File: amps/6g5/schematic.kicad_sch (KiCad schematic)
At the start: 98 parts, among them SW1 AC

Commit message: Fix: 6G5 tone network redrawn from the A-FJ sheet — it is the 6G4's, part for part; taper letters corrected
- The sheet draws the 6G4 network exactly: .05 coupler, 100K slope, 250MM
  treble capacitor, a Bass DIVIDER with .01 across its upper section and 10K
  across its lower, the Treble wiper into the Volume pot, 47MM across it.
- The drawing had no slope resistor and no coupler, and put the 10K in series
  with the .01 between the plate and the stack — while bom.yaml's own role for
  that 10K read "tone network foot". Parts list and drawing contradicted each
  other about the same part.
- Parts list: CC1T/CC2T .05, RS1T/RS2T 100K, CBR1/CBR2 47 pF added; CF/RF roles
  rewritten. And two taper letters corrected to what BOTH pages of the drawing
  print: Treble 250K-L (was 250 kΩ-A) and Volume 500K-L (was 250 kΩ-A, with a
  note about "two candidate tapers" that the sheet does not carry). Every
  surface agrees (check_value_consistency --strict clean).
- Board: this layout placed no tone parts at all ("schematic-only"). Now the
  couplers stand at the plate eyelets and the Treble and Bass pots and the
  parts the layout page hangs at each pot are drawn on the panel row and wired
  lug to lug; the board is widened to 51 columns so the two control groups fit
  without moving any existing board part. Hand-routed to zero findings, then
  tidied by the route helper (which also eased seven pre-existing leads in the
  output section by a fraction of a column). verify_layout_nets PASS (claimed).
- Circuit story: the network as the sheet draws it, the taper correction
  recorded, and the three repo-path leaks (voltages.yaml ×2, netlist.cir)
  rewritten in visitor voice; the sheet notes likewise.
- Social cards and their manifest regenerated for all three repaired boards.

Co-Authored-By: Claude Fable 5.1 <noreply@anthropic.com>
Claude-Session: https://claude.ai/code/session_01KBMfdh37HmCL2iWcBiL5J1
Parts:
- removed CF4: 20u 600V, symbol cx:C
- removed CFB1: .0025u, symbol cx:C
- removed CT2: 250p, symbol cx:C
- removed R2N: 68k, symbol cx:R
- removed RD1: 56k 1W, symbol cx:R
- removed RF2: 10k, symbol cx:R
- removed RG2A, RG5: 1M, symbol cx:R
- removed RPRES: 1.5k, symbol cx:R
- removed V1B, V3, V5, V6A: 7025, symbol cx:TRIODE
- removed V7: 6L6GC, symbol cx:PENTODE
- added CBR1, CBR2: 47p, symbol cx:C
- added CC2T: .05u, symbol cx:C
- added CF2, CTO1: .01u, symbol cx:C
- added CF6: 20u 600V, symbol cx:C
- added CK1B: 25u (info.), symbol cx:C
- added CPRES: .1u 200V, symbol cx:C
- added CT1: 250p, symbol cx:C
- added JSPK: spkr, symbol cx:JACK
- added RFB1: 470k, symbol cx:R
- added RGA: 1M, symbol cx:R
- added RK2A, RK5: 820, symbol cx:R
- added RS1T, RTOP: 100k, symbol cx:R
- added SW1: AC, symbol cx:SWITCH
- added V2A: 7025, symbol cx:TRIODE
- added VRB2: 250k-A, symbol cx:POT
- added VRSPD: 4M-RA speed, symbol cx:POT
- CC1T: renamed from CT1; value 250p -> .05u
- CFB1: renamed from CTO1; value .01u -> .0025u
- CMIX2: renamed from RK5; value 820 -> .05u; symbol cx:R -> cx:C
- CT2: renamed from CF2; value .01u -> 250p
- R2N: renamed from V2A; value 7025 -> 68k; symbol cx:TRIODE -> cx:R
- RD1: renamed from SW1; value AC -> 56k 1W; symbol cx:SWITCH -> cx:R
- RF2: renamed from RL2B; value 100k -> 10k
- RFB2: renamed from RTOP; value 100k -> 220k
- RG2A: renamed from RK2A; value 820 -> 1M
- RG5: renamed from RFB1; value 470k -> 1M
- RL2B: renamed from CMIX2; value .05u -> 100k; symbol cx:C -> cx:R
- RPRES: renamed from RGA; value 1M -> 1.5k
- RS2T: renamed from VRB2; value 250k-A -> 100k; symbol cx:POT -> cx:R
- RSC2: renamed from JSPK; value spkr -> 470 1W; symbol cx:JACK -> cx:R
- RTAIL: renamed from CPRES; value .1u 200V -> 820; symbol cx:C -> cx:R
- V1B: renamed from CK1B; value 25u (info.) -> 7025; symbol cx:C -> cx:TRIODE
- V3: renamed from VRSPD; value 4M-RA speed -> 7025; symbol cx:POT -> cx:TRIODE
- V5: renamed from RFB2; value 220k -> 7025; symbol cx:R -> cx:TRIODE
- V6A: renamed from RTAIL; value 820 -> 7025; symbol cx:R -> cx:TRIODE
- V7: renamed from RSC2; value 470 1W -> 6L6GC; symbol cx:R -> cx:PENTODE
- VRT1, VRT2: value 250k-A -> 250k-L
- VRV1, VRV2: value 250k-A -> 500k-L
- renumbered CF6 to CF4
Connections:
- net BD: now also RL2B.1; no longer RF2.1
- net BP1: now also CF4.1, RTOP.1; no longer RFB2.1
- net BP2: now also RD1.1, RSC2.2; no longer V7.2
- net BP3: now also RD1.2, CF6.1; no longer CF4.1
- net BRT 1: now also RG2A.1, V2A.2 (G)
- net BRT 2: now also R2N.1
- net GND: now also CFB1.1, RF1.2, RF2.2, RFB2.2, RG5.2, RPRES.2, V7.4 (K), CF6.2, CK1B.2, CPRES.2, RK2A.2, RK5.2, VRB2.3, VRSPD.1, VRSPD.2 (W); no longer CMIX2.2, RS2T.3, RTAIL.2, V1B.2, V3.1, V3.2 (W), V5.2
- net MAINS: now also SW1.1; no longer RD1.1
- net MIXG2: now also CMIX2.2, RG5.1, V5.2 (G); no longer RL2B.2
- net SPKR: now also JSPK.1 (T); no longer RSC2.1 (T)
- net at TR2.5 (SEC_C): now also JSPK.2 (S); no longer RSC2.2 (S)
- net at CTOK.1, D1.1 (A), D2.1 (A)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: now also V3.3 (K)
- net at V2B.2 (G), VRV2.2 (W): now also CBR2.2
- net at F1.1: now also SW1.2; no longer RD1.2
- net at CC1T.1, RL1A.2, V1A.1 (P): no longer RF1.1
- net at RL2A.2: now also CC2T.1, V2A.1 (P); no longer R2N.1 (P)
- net at CMIX2.1: now also RL2B.2, V2B.1 (P); no longer CK5.1
- net at CFB1.2: now also RL5.2, V5.1 (P), RFB1.1; no longer V3.3
- net at CF1.1: now also VRB1.1, VRT1.3, RS1T.2; no longer RF1.2
- net at CTO2.1, RTOG2.2: now also V3.2 (G)
- net at CTO2.2, RTOG1.2: now also CTO1.1; no longer CFB1.1
- net at V8.3 (G2): now also RSC2.1; no longer V7.1
- net at CTO3.2, VRINT.1: now also V3.1 (P), RTOP.2; no longer RFB2.2
- net at CMIX1.1, RL1B.2: now also V1B.1 (P)
- net at RPRES.1: now also RNFB.2, RT2.1, VRPRES.1, VRPRES.2 (W)
- net at RGB.1, RT2.2: now also RTAIL.1, RGA.2; no longer RPRES.2, V6A.1
- net at RK1B.1: now also V1B.3 (K), CK1B.1; no longer V1B.1
- net at VRV1.1: now also CBR1.1; no longer VRT1.2 (W)
- net at VRV1.2 (W): now also V1B.2 (G), CBR1.2
- net at C1.1, CPID.1, RLA.2: now also V6A.1 (P)
- net at C1.2, RGL1.1: now also V7.2 (G1)
- net at V6B.3 (K): now also RTAIL.2, V6A.3 (K); no longer V6A.2
- net at VRPRES.3: now also CPRES.1; no longer RTAIL.1
- net at VRT2.1: now also CT2.2
- net at CC1T.2: now also CT1.1, RS1T.1; no longer VRT1.1
- net at TR2.1 (PRI_A): now also V7.1 (P)
- net at VRT2.2 (W): no longer VRV2.1
- net at RS2T.2, VRT2.3: now also CF2.1, VRB2.1; no longer RS2T.1
- net at CF1.2: now also RF1.1, VRB1.2 (W)
- net at RSC1.1: now also V7.3 (G2)
- net at CT2.1: now also RS2T.1, CC2T.2
- new net: RFB1.2, RFB2.1, RFB3.2
- new net: CTO1.2, VRSPD.3
- new net: RGA.1, V6A.2 (G)
- new net: CF2.2, RF2.1, VRB2.2 (W)
- new net: CT1.2, VRT1.1
- new net: CBR2.1, VRV2.1
- new net: CK2A.1, RK2A.1, V2A.3 (K)
- new net: CK5.1, RK5.1, V5.3 (K)
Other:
- note added: "Bias supply — a filtered tap this drawing does not fully resolve; the netlist treats -55 V as an ideal source (see the circuit story)"
- note added: "Driver — local feedback network read from the drawing but not confidently resolved (schematic-only; see the circuit story and the parts list)"
- note added: "Heaters, PT primary/mains, pilot lamp and chassis switches are omitted here — see the netlist, the sources list and the board drawing. BP3/BDRV/BD are DRIVEN anchors, not derived through the dropper chain shown (see the circuit story)."
- note added: "Mains cord not drawn — annotation layer (see the board drawing)"
- note added: "Phase-shift ladder values (RTOG1/RTOG2/CTO1-3) are a schematic-only reading, typical of this circuit family — not confidently resolved from the scan (see the parts list)."
- note added: "Pilot lamp — fed from the 6.3 V heater chain (the board drawing's twisted pair)"
- note added: "The tremolo oscillator drives a lamp/photoresistor pair (OPTO) whose photocell shunts the channel-mixing node (see the circuit story)."
- note added: "Tremolo — V3 phase-shift oscillator (DC point excluded from the netlist)"
- note removed: "Bias supply — a filtered tap this drawing does not fully resolve; netlist.cir treats -55 V as an ideal source (notes.md)"
- note removed: "Driver — local feedback network read from the drawing but not confidently resolved (schematic-only; see notes.md, bom.yaml)"
- note removed: "Heaters, PT primary/mains, pilot lamp and chassis switches are omitted here — see netlist.cir, meta.yaml, layout.yaml. BP3/BDRV/BD are DRIVEN anchors, not derived through the dropper chain shown (notes.md)."
- note removed: "Mains cord not drawn — annotation layer (layout.yaml)"
- note removed: "Phase-shift ladder values (RTOG1/RTOG2/CTO1-3) are a schematic-only reading, typical of this circuit family — not confidently resolved from the scan (bom.yaml)."
- note removed: "Pilot lamp — fed from the 6.3 V heater chain (layout.yaml twisted run)"
- note removed: "The tremolo oscillator drives a lamp/photoresistor pair (OPTO) whose photocell shunts the channel-mixing node (notes.md)."
- note removed: "Tremolo — V3 phase-shift oscillator (DC point excluded from netlist.cir)"
- moved on the sheet: CC1T, CF4, CFB1, CK1A, CT2, R1N, RF2, RFB2, RG1A, RG2A, RG5, RK1A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

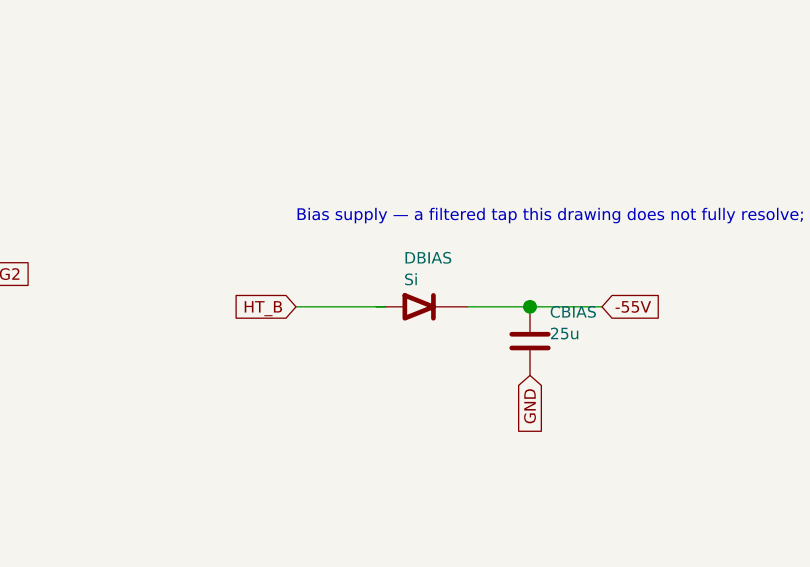
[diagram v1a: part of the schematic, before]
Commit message: Fix: 17 bias rectifiers and six HT diodes drawn backwards; the 6G6-B and 6G4 bias rows as their drawings show; AA1164 V4 units
Rectifier polarity has no gate. The netlists model every supply as an ideal
source, the sheet-vs-board check treats a two-terminal part as unordered, and
the boards' `cathode:` fields were copied from the sheets. Measured over all
68 diodes on 40 sheets: 18 negative-bias rectifiers had the cathode on the
negative node (a diode that way round would charge the node POSITIVE), and all
six 6G6-B HT diodes pointed away from B+. The printed negative bias on each of
those sheets falsifies the drawn orientation; the nine bias rectifiers already
right (AA1164, AA864, AB165, B15N, DR103, JTM100, M1959, M2204, 6G6-B) show
the idiom. Flipped: 5E4-A, 5E5-A, 5E6-A, 5F10, 5F4, 5F6, 5F6-A, 5F8-A, 5G9,
6G2, 6G3, 6G4, 6G5, AA964, AB763, AB763 Super, AB763 Twin, JTM45 (the
M1987's is with the Marshall board repair) and the 6G6-B's DR1-DR6. The
5F8-A board, which had copied its sheet, has the band moved to the tap side;
the other boards' bands are with the board-repair wave. A gate is next.

6G6-B bias. E-FB (6431x3364): the 1K 1W rises from TR1's SECOND secondary
terminal, a bias tap between the upper HT end and the grounded centre tap,
to the diode's + end. The sheet fed the diode from the HT end with the 1K
after it. T1 now carries its tap pin and the row reads tap -> 1K -> diode ->
-54 V. (The triage had read "HT end"; the native crop shows the tap.)

6G4 bias. A-FJ, read natively: tap -> rectifier -> 8 uF -> 10K -> the -55 V
node, which carries a second 8 uF and the 56K to ground as a bleeder. The
sheet fed the rectifier from an HT end, drew the 56K in series and carried
one capacitor. CBIAS2 joins the parts list, and RBIAS1's role now says
bleeder.

AA1164 V4. The K-FD sheet prints the phase inverter 7/6/8 and the tremolo
oscillator 2/1/3 (5554x4346); the sheet had them the other way round.

Gates: check_schematics 40/0 (+selftest), verify_schematic_nets 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
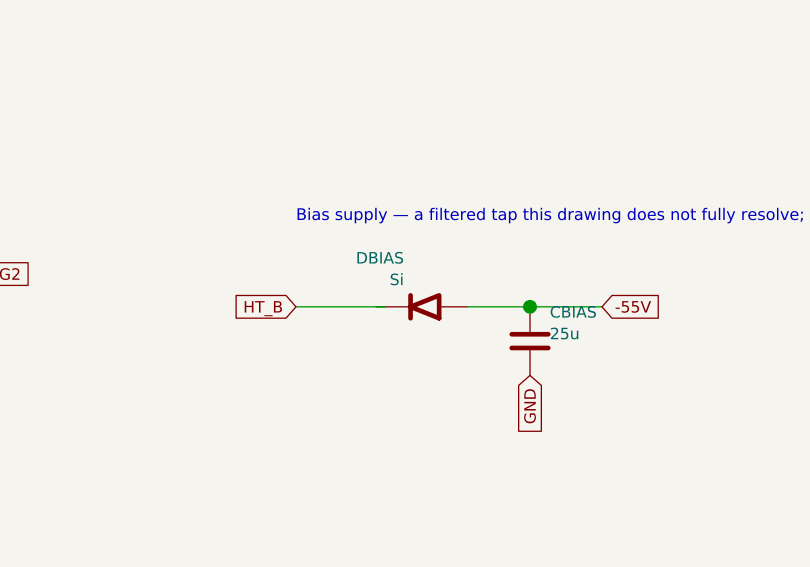
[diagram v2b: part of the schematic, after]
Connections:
- net -55V: now also DBIAS.1 (A); no longer DBIAS.2 (K)
- net HT_B: now also DBIAS.2 (K); no longer DBIAS.1 (A)
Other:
- moved on the sheet: DBIAS
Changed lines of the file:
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@@
   (wire (pts (xy 215.665 206.889) (xy 216.745 206.889))
     (stroke (width 0) (type default)))
-  (symbol (lib_id "cx:DIODE_SS") (at 220.745 206.889 0) (unit 1)
+  (symbol (lib_id "cx:DIODE_SS") (at 220.745 206.889 180) (unit 1)
     (in_bom yes) (on_board yes)
     (property "Reference" "DBIAS" (at 218.745 201.489 0) (effects (font (size 1.27 1.27)) (justify left)))

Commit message: Fix: the 6G5's rectifier was connected to nothing; 17 sheets shorted the mains by naming both leads alike
6G5 power supply. The sheet drew four diodes as a "silicon bridge" whose
HT_A/HT_B labels stopped 6 mm short of their wires. D1/D2's anodes sat on
the tremolo's cathode node (a tremolo wire's end touched the old diode
stub), D3/D4 ran from ground to the reservoir, and TR1's centre tap floated
under an open-pin waiver whose stated reason was the bridge itself.
A-FJ (Schematic Heaven 2153x1437, read enlarged): each HT end of TR1 runs
through a leg of three silicon diodes, every + (cathode) toward the +460 V
reservoir; the centre tap is grounded; TR1's second secondary terminal is a
bias tap feeding the 6G4's network part for part: rectifier, 8-150, 10K,
then 8-150 and a 56K bleeder at the -55 V line. Redrawn as the drawing
shows: D1-D6, TR1 with its tap pin, the centre tap to ground, the bias
network (CBIAS 25 uF -> 8 uF; RBIAS2, CBIAS2, RBIAS1 added), the waiver
deleted, and the notes, meta, netlist header and parts list no longer say
bridge. Not yet carried: the drawing's second 20-600 at the reservoir and
the standby switch (this sheet omits chassis switches by its own note);
and the tremolo ladder still runs through the transformer's corner of the
sheet, a layout clash rather than a connection, queued for its own redraw.

Mains. Two global labels with one name are one net. 16 of 24 power
transformers on the sheets carried a label named MAINS on both primary
leads, so the winding's two pins were one net: 5E4-A, 5E5-A, 5F4, 5G9,
6161, 6G2, 6G3, 6G4, AA1164, AA764, AA764-Vibro, AA964, AB763, AB763
Super, AB763 Twin, GA-40. The 6G5's loop ran from one MAINS label through
switch, fuse and winding back to the same name. No gate models the primary,
so a copy-pasted idiom did this. The second lead is now MAINS N, the AC15's
idiom; the AA1164's and AA964's second AC row, drawn under the first row's
name, is the neutral. The death and across-the-line caps stay on the le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
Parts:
- removed CF3: 20u 600V, symbol cx:C
- removed CTOK: 25u+25u, symbol cx:C
- removed D2: 1N4007, symbol cx:DIODE_SS
- removed DBIAS: Si, symbol cx:DIODE_SS
- removed F1: 3A, symbol cx:FUSE
- removed TR1: n/a, symbol cx:PT
- removed V6B: 7025, symbol cx:TRIODE
- added CBIAS2: 8u, symbol cx:C
- added CF6, CF7: 20u 600V, symbol cx:C
- added D1, D4, D5, D6: 1N4007, symbol cx:DIODE_SS
- added PL1: pilot, symbol cx:LAMP
- added RBIAS1: 56k, symbol cx:R
- added RBIAS2: 10k, symbol cx:R
- added RTOK: 1.5k, symbol cx:R
- added V6A: 7025, symbol cx:TRIODE
- CBIAS: value 25u -> 8u
- CF3: renamed from D4; value 1N4007 -> 20u 600V; symbol cx:DIODE_SS -> cx:C
- CTOK: renamed from RTOK; value 1.5k -> 25u+25u; symbol cx:R -> cx:C
- DBIAS: renamed from PL1; value pilot -> Si; symbol cx:LAMP -> cx:DIODE_SS
- F1: renamed from CF7; value 20u 600V -> 3A; symbol cx:C -> cx:FUSE
- TR1: renamed from CF6; value 20u 600V -> n/a; symbol cx:C -> cx:PT
- renumbered D1 to D2, V6A to V6B
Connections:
- net -55V: now also CBIAS2.1, RBIAS1.1, RBIAS2.2; no longer CBIAS.1
- net BD: now also CF7.1; no longer F1.1
- net BP3: now also CF6.1; no longer TR1.1
- net B_RES: now also CF3.1, D6.2 (K); no longer CF3.2 (K)
- net GND: now also CF3.2, TR1.4 (HT_CT), CBIAS2.2, CF6.2, CF7.2, RBIAS1.2, RTOK.2; no longer CF3.1 (A), D2.2 (K), D3.1 (A), F1.2, TR1.2
- net HTR_A: now also PL1.1; no longer DBIAS.1
- net HTR_B: now also PL1.2; no longer DBIAS.2
- net HT_A: now also TR1.3 (HT_A), D1.1 (A)
- net HT_B: now also TR1.5 (HT_B), D4.1 (A)
- net at CBR1.1, VRV1.1: now also VRT1.2 (W)
- net at CF1.2, RF1.1: no longer VRB1.2 (W)
- net at CTOK.1, RTOG1.1, V3.3 (K): now also RTOK.1; no longer D2.1 (A)
- net at RGB.2: now also V6B.2 (G)
- net at C2.1, CPID.2, RLB.2: now also V6B.1 (P)
- net at C1.1, CPID.1, RLA.2: now also V6A.1 (P); no longer V6B.1 (P)
- net at RTAIL.2, V6B.3 (K): now also V6A.3 (K)
- net at RGA.1: now also V6A.2 (G); no longer V6B.2 (G)
- net at CF2.2, RF2.1: no longer VRB2.2 (W)
- net at VRT2.2 (W): now also CBR2.1, VRV2.1
- net at SW1.2: now also F1.1
- new net: D5.2 (K), D6.1 (A)
- new net: F1.2, TR1.1 (PRI_1)
- new net: D4.2 (K), D5.1 (A)
- new net: D1.2 (K), D2.1 (A)
- new net: D2.2 (K), D3.1 (A)
- new net: CBIAS.1, DBIAS.1 (A), RBIAS2.1
- new net HT_TAP: DBIAS.2 (K), TR1.6 (HT_TAP)
- new net MAINS N: TR1.2 (PRI_2)
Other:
- note added: "Bias supply — TR1's bias tap, a rectifier, 8 uF, 10k, then 8 uF with a 56k bleeder, to -55 V (the netlist drives the -55 V line as an ideal source)"
- note added: "Power supply — silicon full-wave: two legs of three diodes off the centre-tapped HT winding (no tube rectifier); TR1 power, TR2 output (drawing's own designators)"
- note removed: "Bias supply — a filtered tap this drawing does not fully resolve; the netlist treats -55 V as an ideal source (see the circuit story)"
- note removed: "Power supply — silicon full-wave bridge off a single HT secondary (no tube rectifier); TR1 power, TR2 output (drawing's own designators)"
- moved on the sheet: CBR1, CBR2, CC1T, CC2T, CF1, CF2, CF3, CFB1, CK1A, CK1B, CK2A, CK2B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
